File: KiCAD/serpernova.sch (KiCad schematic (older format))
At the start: 121 parts, among them Q1 2N3904, Q10 2N7000, Q2 2N3906, Q3 2N7000, Q4 2N7000, Q5 2N7000, Q6 2N7000, Q7 2N7000, Q8 2N7000, Q9 2N7000, U1 STM8S105K6B6

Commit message: Travail sur supernova.f
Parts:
- removed R12, R14, R15, R17, R20, R22, R23, R25, R28, R30, R31, R33, R36, R38, R7, R9: 150, symbol Device:R
- R10, R11, R13, R16, R18, R19, R21, R24, R26, R27, R29, R32, R34, R35, R37, R8: value 150 -> 20
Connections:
- net at D51.1 (K), D52.1 (K): now also D53.1 (K), D54.1 (K), R32.1
- net at D55.1 (K), D56.1 (K): now also D57.1 (K), D58.1 (K), R34.1
- net at D43.1 (K), D44.1 (K), R27.2: now also D45.1 (K), D46.1 (K)
- net at D47.1 (K), D48.1 (K), R29.2: now also D49.1 (K), D50.1 (K)
- net at D35.1 (K), D36.1 (K): now also D37.1 (K), D38.1 (K), R24.1
- net at D39.1 (K), D40.1 (K): now also D41.1 (K), D42.1 (K), R26.1
- net at D27.1 (K), D28.1 (K), R19.2: now also D29.1 (K), D30.1 (K)
- net at D31.1 (K), D32.1 (K), R21.2: now also D33.1 (K), D34.1 (K)
- net at D19.1 (K), D20.1 (K): now also D21.1 (K), D22.1 (K), R16.1
- net at D23.1 (K), D24.1 (K): now also D25.1 (K), D26.1 (K), R18.1
- net at D59.1 (K), D60.1 (K), R35.2: now also D61.1 (K), D62.1 (K)
- net at D63.1 (K), D64.1 (K), R37.2: now also D65.1 (K), D66.1 (K)
- net at D11.1 (K), D12.1 (K), R11.2: now also D13.1 (K), D14.1 (K)
- net at D15.1 (K), D16.1 (K), R13.2: now also D17.1 (K), D18.1 (K)
- net at D3.1 (K), D4.1 (K): now also D5.1 (K), D6.1 (K), R8.1
- net at D7.1 (K), D8.1 (K): now also D10.1 (K), D9.1 (K), R10.1

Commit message: modification à la schématique
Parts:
- renumbered R13 to R10, R16 to R11, R18 to R12, R19 to R13, R21 to R14, R24 to R15, R26 to R16, R27 to R17, R29 to R18, R32 to R19, R34 to R20, R35 to R21, R37 to R22, R8 to R7, R10 to R8, R11 to R9
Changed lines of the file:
@@
 $EndComp
 $Comp
-L Device:R R8
+L Device:R R7
 U 1 1 5F8C4390
 P 4700 3400
-F 0 "R8" H 4770 3446 50  0000 L CNN
+F 0 "R7" H 4770 3446 50  0000 L CNN
 F 1 "20" H 4770 3355 50  0000 L CNN
 F 2 "" V 4630 3400 50  0001 C CNN
@@
 $EndComp
 $Comp
-L Device:R R10
+L Device:R R8
 U 1 1 5F8C7C7E
 P 4700 5000
-F 0 "R10" H 4770 5046 50  0000 L CNN
+F 0 "R8" H 4770 5046 50  0000 L CNN
 F 1 "20" H 4770 4955 50  0000 L CNN
 F 2 "" V 4630 5000 50  0001 C CNN
@@
 Connection ~ 4700 5150
 $Comp
-L Device:R R11
+L Device:R R9
 U 1 1 5F9039ED
 P 5800 2150
-F 0 "R11" H 5870 2196 50  0000 L CNN
-F 1 "20" H 5870 2105 50  0000 L CNN
+F 0 "R9" H 5750 1850 50  0000 L CNN
+F 1 "20" H 5750 1950 50  0000 L CNN
 F 2 "" V 5730 2150 50  0001 C CNN
 F 3 "~" H 5800 2150 50  0001 C CNN
@@
 $EndComp
 $Comp
-L Device:R R13
+L Device:R R10
 U 1 1 5F904C15
 P 5800 3900
-F 0 "R13" H 5870 3946 50  0000 L CNN
-F 1 "20" H 5870 3855 50  0000 L CNN
+F 0 "R10" H 5750 4150 50  0000 L CNN
+F 1 "20" H 5800 4050 50  0000 L CNN
 F 2 "" V 5730 3900 50  0001 C CNN
 F 3 "~" H 5800 3900 50  0001 C CNN
@@
 $EndComp
 $Comp
-L Device:R R18
+L Device:R R12
 U 1 1 5F94713C
 P 6400 4950
-F 0 "R18" H 6470 4996 50  0000 L CNN
-F 1 "20" H 6470 4905 50  0000 L CNN
+F 0 "R12" H 6450 4900 50  0000 L CNN
+F 1 "20" H 6450 4800 50  0000 L CNN
 F 2 "" V 6330 4950 50  0001 C CNN
 F 3 "~" H 6400 4950 50  0001 C CNN
@@
 $EndComp
 $Comp
-L Device:R R16
+L Device:R R11
 U 1 1 5F94933C
 P 6400 3350
-F 0 "R16" H 6470 3396 50  0000 L CNN
-F 1 "20" H 6470 3305 50  0000 L CNN
+F 0 "R11" H 6350 3050 50  0000 L CNN
+F 1 "20" H 6350 3150 50  0000 L CNN
 F 2 "" V 6330 3350 50  0001 C CNN
 F 3 "~" H 6400 3350 50  0001 C CNN
@@
 $EndComp
 $Comp
-L Device:R R19
+L Device:R R13
 U 1 1 5F9E6919
 P 7100 2150
-F 0 "R19" H 7170 2196 50  0000 L CNN
-F 1 "20" H 7170 2105 50  0000 L CNN
+F 0 "R13" H 7100 2300 50  0000 L CNN
+F 1 "20" H 7150 2200 50  0000 L CNN
 F 2 "" V 7030 2150 50  0001 C CNN
 F 3 "~" H 7100 2150 50  0001 C CNN
@@
 $EndComp
 $Comp
-L Device:R R21
+L Device:R R14
 U 1 1 5FA18F1B
 P 7150 3900
-F 0 "R21" H 7220 3946 50  0000 L CNN
-F 1 "20" H 7220 3855 50  0000 L CNN
+F 0 "R14" H 7100 4100 50  0000 L CNN
+F 1 "20" H 7200 3950 50  0000 L CNN
 F 2 "" V 7080 3900 50  0001 C CNN
 F 3 "~" H 7150 3900 50  0001 C CNN
@@
 Connection ~ 8050 2300
 $Comp
-L Device:R R24
+L Device:R R15
 U 1 1 5FA92B84
 P 7800 3350
-F 0 "R24" H 7870 3396 50  0000 L CNN
+F 0 "R15" H 7870 3396 50  0000 L CNN
 F 1 "20" H 7870 3305 50  0000 L CNN
 F 2 "" V 7730 3350 50  0001 C CNN
@@
 $EndComp
 $Comp
-L Device:R R26
+L Device:R R16
 U 1 1 5FA94099
 P 7800 4950
-F 0 "R26" H 7870 4996 50  0000 L CNN
+F 0 "R16" H 7870 4996 50  0000 L CNN
 F 1 "20" H 7870 4905 50  0000 L CNN
 F 2 "" V 7730 4950 50  0001 C CNN
@@
 	7700 3500 7800 3500
 $Comp
-L Device:R R34
+L Device:R R20
 U 1 1 5FB1AE05
 P 9500 4950
-F 0 "R34" H 9570 4996 50  0000 L CNN
-F 1 "20" H 9570 4905 50  0000 L CNN
+F 0 "R20" H 9550 4950 50  0000 L CNN
+F 1 "20" H 9550 4850 50  0000 L CNN
 F 2 "" V 9430 4950 50  0001 C CNN
 F 3 "~" H 9500 4950 50  0001 C CNN
@@
 $EndComp
 $Comp
-L Device:R R32
+L Device:R R19
 U 1 1 5FB1C712
 P 9500 3350
-F 0 "R32" H 9570 3396 50  0000 L CNN
-F 1 "20" H 9570 3305 50  0000 L CNN
+F 0 "R19" H 9550 3350 50  0000 L CNN
+F 1 "20" H 9550 3250 50  0000 L CNN
 F 2 "" V 9430 3350 50  0001 C CNN
 F 3 "~" H 9500 3350 50  0001 C CNN
@@
 $EndComp
 $Comp
-L Device:R R35
+L Device:R R21
 U 1 1 5FB1E1EB
 P 10200 2150
-F 0 "R35" H 10270 2196 50  0000 L CNN
-F 1 "20" H 10270 2105 50  0000 L CNN
+F 0 "R21" H 10200 2350 50  0000 L CNN
+F 1 "20" H 10250 2200 50  0000 L CNN
 F 2 "" V 10130 2150 50  0001 C CNN
 F 3 "~" H 10200 2150 50  0001 C CNN
@@
 $EndComp
 $Comp
-L Device:R R37
+L Device:R R22
 U 1 1 5FB332EA
 P 10200 3900
-F 0 "R37" H 10270 3946 50  0000 L CNN
-F 1 "20" H 10270 3855 50  0000 L CNN
+F 0 "R22" H 10150 4100 50  0000 L CNN
+F 1 "20" H 10250 3950 50  0000 L CNN
 F 2 "" V 10130 3900 50  0001 C CNN
 F 3 "~" H 10200 3900 50  0001 C CNN
@@
 $EndComp
 $Comp
-L Device:R R27
+L Device:R R17
 U 1 1 5FC05558
 P 8600 2150
-F 0 "R27" H 8670 2196 50  0000 L CNN
+F 0 "R17" H 8650 2200 50  0000 L CNN
 F 1 "20" H 8670 2105 50  0000 L CNN
 F 2 "" V 8530 2150 50  0001 C CNN
@@
 $EndComp
 $Comp
-L Device:R R29
+L Device:R R18
 U 1 1 5FC07D69
 P 8600 3900
-F 0 "R29" H 8670 3946 50  0000 L CNN
+F 0 "R18" H 8650 3950 50  0000 L CNN
 F 1 "20" H 8670 3855 50  0000 L CNN
 F 2 "" V 8530 3900 50  0001 C CNN

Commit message: travail sur base modifié schématique
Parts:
- C1: value CP -> 10µF/25v
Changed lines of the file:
@@
 P 1700 3200
 F 0 "C1" H 1582 3154 50  0000 R CNN
-F 1 "CP" H 1582 3245 50  0000 R CNN
+F 1 "10µF/25v" H 1582 3245 50  0000 R CNN
 F 2 "" H 1738 3050 50  0001 C CNN
 F 3 "~" H 1700 3200 50  0001 C CNN

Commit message: mise à jour schématique
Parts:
- added J1: interface, symbol Connector:Conn_01x07_Male
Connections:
- net +5V: now also J1.4 (Pin_4)
- net GND: now also J1.3 (Pin_3), J1.5 (Pin_5)
- net RS232_RX: now also J1.7 (Pin_7)
- net RS232_TX: now also J1.6 (Pin_6)
- net SWIM: now also J1.2 (Pin_2)
- net ~rst: now also J1.1 (Pin_1)
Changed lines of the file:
@@
 	10200 4800 10200 4050
 Connection ~ 10200 4050
+$Comp
+L Connector:Conn_01x07_Male J1
+U 1 1 5F84B0EE
+P 850 4050
+F 0 "J1" H 958 4531 50  0000 C CNN
+F 1 "interface" V 750 4050 50  0000 C CNN
+F 2 "" H 850 4050 50  0001 C CNN
+F 3 "~" H 850 4050 50  0001 C CNN
+	1    850  4050
+	1    0    0    -1
+$EndComp
+Text Label 1050 4050 0    50   ~ 0
++5V
+$Comp
+L power:GND #PWR?
+U 1 1 5F8566E6
+P 1600 4150
+F 0 "#PWR?" H 1600 3900 50  0001 C CNN
+F 1 "GND" H 1605 3977 50  0000 C CNN
+F 2 "" H 1600 4150 50  0001 C CNN
+F 3 "" H 1600 4150 50  0001 C CNN
+	1    1600 4150
+	1    0    0    -1
+$EndComp
+Text Label 1050 3850 0    50   ~ 0
+SWIM
+Text Label 1050 3750 0    79   ~ 0
+~rst
+Text Label 1050 4250 0    50   ~ 0
+RS232_TX
+Text Label 1050 4350 0    50   ~ 0
+RS232_RX
+Wire Wire Line
+	1050 4150 1600 4150
+Wire Wire Line
+	1600 3950 1600 4150
+Wire Wire Line
+	1050 3950 1600 3950
+Connection ~ 1600 4150
 $EndSCHEMATC

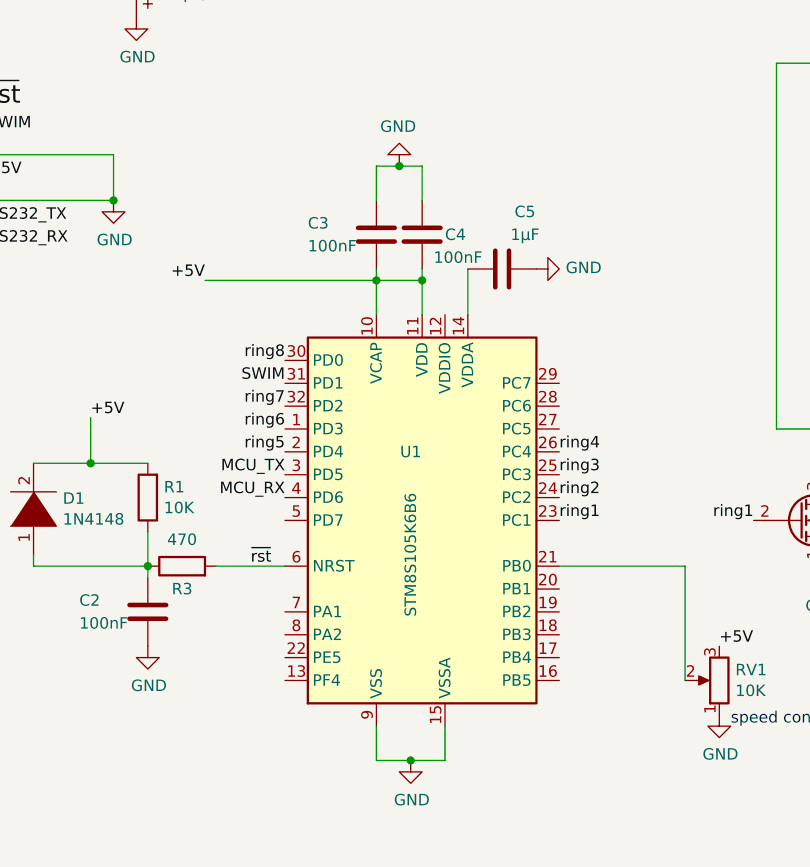
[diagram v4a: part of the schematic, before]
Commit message: correction schématique!
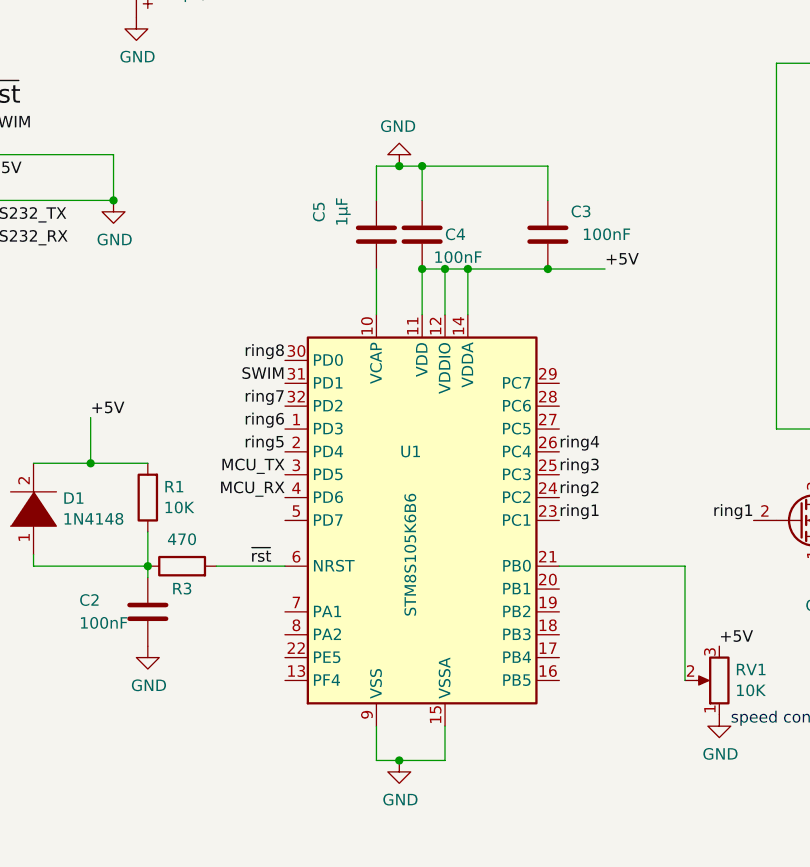
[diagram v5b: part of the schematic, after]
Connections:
- net +5V: now also U1.12 (VDDIO), U1.14 (VDDA); no longer U1.10 (VCAP)
- net at C5.2: now also U1.10 (VCAP); no longer U1.14 (VDDA)
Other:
- moved on the sheet: C3, C5
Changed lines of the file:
@@
 L Device:C C5
 U 1 1 5FD06AD8
-P 3300 4450
-F 0 "C5" V 3050 4550 50  0000 C CNN
-F 1 "1µF" V 3150 4550 50  0000 C CNN
-F 2 "" H 3338 4300 50  0001 C CNN
-F 3 "~" H 3300 4450 50  0001 C CNN
-	1    3300 4450
-	0    1    1    0
+P 2750 4300
+F 0 "C5" V 2500 4400 50  0000 C CNN
+F 1 "1µF" V 2600 4400 50  0000 C CNN
+F 2 "" H 2788 4150 50  0001 C CNN
+F 3 "~" H 2750 4300 50  0001 C CNN
+	1    2750 4300
+	1    0    0    -1
 $EndComp
 Wire Wire Line
@@
 $EndComp
 $Comp
-L power:GND #PWR06
-U 1 1 5FD22DF2
-P 3450 4450
-F 0 "#PWR06" H 3450 4200 50  0001 C CNN
-F 1 "GND" V 3455 4322 50  0000 R CNN
-F 2 "" H 3450 4450 50  0001 C CNN
-F 3 "" H 3450 4450 50  0001 C CNN
-	1    3450 4450
-	0    -1   -1   0
-$EndComp
-$Comp
 L Device:C C3
 U 1 1 5FD23880
-P 2750 4300
-F 0 "C3" H 3050 4250 50  0000 R CNN
-F 1 "100nF" H 3050 4350 50  0000 R CNN
-F 2 "" H 2788 4150 50  0001 C CNN
-F 3 "~" H 2750 4300 50  0001 C CNN
-	1    2750 4300
+P 3500 4300
+F 0 "C3" H 3400 4200 50  0000 R CNN
+F 1 "100nF" H 3350 4300 50  0000 R CNN
+F 2 "" H 3538 4150 50  0001 C CNN
+F 3 "~" H 3500 4300 50  0001 C CNN
+	1    3500 4300
 	-1   0    0    1
 $EndComp
@@
 	-1   0    0    1
 $EndComp
-Wire Wire Line
-	2750 4450 2750 4500
-Wire Wire Line
-	2950 4450 2950 4500
 $Comp
 L power:GND #PWR04
@@
 L power:GND #PWR05
 U 1 1 5FD8D17D
-P 2900 6600
-F 0 "#PWR05" H 2900 6350 50  0001 C CNN
-F 1 "GND" H 2905 6427 50  0000 C CNN
-F 2 "" H 2900 6600 50  0001 C CNN
-F 3 "" H 2900 6600 50  0001 C CNN
-	1    2900 6600
+P 2850 6600
+F 0 "#PWR05" H 2850 6350 50  0001 C CNN
+F 1 "GND" H 2855 6427 50  0000 C CNN
+F 2 "" H 2850 6600 50  0001 C CNN
+F 3 "" H 2850 6600 50  0001 C CNN
+	1    2850 6600
 	1    0    0    -1
 $EndComp
@@
 	2750 6450 2750 6600
 Wire Wire Line
-	2750 6600 2900 6600
+	2750 6600 2850 6600
 Wire Wire Line
 	3050 6600 3050 6450
-Connection ~ 2900 6600
-Wire Wire Line
-	2900 6600 3050 6600
 $Comp
 L Device:C C2
@@
 Wire Wire Line
 	1500 5300 1750 5300
-Wire Wire Line
-	2950 4500 2750 4500
-Connection ~ 2950 4500
-Wire Wire Line
-	2950 4500 2950 4650
-Connection ~ 2750 4500
-Wire Wire Line
-	2750 4500 2750 4650
-Text Label 2000 4500 2    50   ~ 0
-+5V
-Wire Wire Line
-	2000 4500 2750 4500
+Text Label 3750 4450 0    50   ~ 0
++5V
 Text Label 6450 1450 2    50   ~ 0
 +5V
@@
 	1050 3950 1600 3950
 Connection ~ 1600 4150
+Connection ~ 2850 6600
+Wire Wire Line
+	2850 6600 3050 6600
+Wire Wire Line
+	3050 4650 3050 4450
+Wire Wire Line
+	3050 4450 3150 4450
+Wire Wire Line
+	2750 4450 2750 4650
+Wire Wire Line
+	2950 4450 2950 4650
+Wire Wire Line
+	2950 4450 3050 4450
+Connection ~ 2950 4450
+Connection ~ 3050 4450
+Wire Wire Line
+	3150 4450 3500 4450
+Connection ~ 3150 4450
+Wire Wire Line
+	2950 4000 3500 4000
+Wire Wire Line
+	3500 4000 3500 4150
+Connection ~ 2950 4000
+Wire Wire Line
+	3500 4450 3750 4450
+Connection ~ 3500 4450
 $EndSCHEMATC
